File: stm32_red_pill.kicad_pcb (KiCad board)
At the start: 2 copper layers, 59 x 31 mm, 29 parts, among them J1 USB_B_Micro, J2 Conn_01x18, J3 Conn_01x18, SW1 SW_SPDT, U1 STM32F103C8T6, U2 AMS1117-3.3, Y1 16MHZ

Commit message: update
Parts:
- removed SW1: SW_SPDT, Button_Switch_SMD:SW_SPDT_PCM12
- added G***: LOGO, LOGO, F.Cu at (89.0, 101.7)
- added J4: Conn_02x02_Top_Bottom, Connector_PinHeader_2.54mm:PinHeader_2x02_P2.54mm_Vertical, F.Cu at (135.9, 96.8)
- moved R1 17.6 mm to (116.0, 100.5), turned to -135 degrees
- moved C7 2.05 mm to (98.3, 103.9), turned to -45 degrees
- moved C11 1.85 mm to (100.8, 96.1)
- moved C10 1.85 mm to (100.8, 94.1)
- moved Y1 1.85 mm to (98.3, 94.9)
- moved R3 1.31 mm to (118.9, 102.5), turned to 135 degrees
- moved FB1 0.90 mm to (97.8, 105.2), turned to -45 degrees
- moved D1 0.68 mm to (119.5, 101.2)
- moved C8 0.21 mm to (97.4, 106.5), turned to 135 degrees
- moved C2 0.06 mm to (111.5, 96.0)
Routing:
- net /SW_BOOT0: track 1.56 -> 21.3 mm, vias 0 -> 2
- net /BOOT0: track 25.6 -> 7.74 mm, vias 2 -> 0
- net +3.3V: track 85.7 -> 93.3 mm
- net /PA2: track 24.1 -> 22.0 mm
- net /HSE_OUT: track 10.1 -> 8.29 mm
- net /HSE_IN: track 13.4 -> 11.5 mm
- net /PA1: track 22.4 -> 20.7 mm
- net GND: track 30.9 -> 29.5 mm, vias 20 -> 24
- net /PA0: track 21.5 -> 20.2 mm
- net +3.3VA: track 12.4 -> 11.4 mm
- net /PB9: track 13.7 -> 14.4 mm, vias 2 -> 0
- net /PA13: track 22.2 -> 22.6 mm, vias 2 -> 1
- net VBUS: track 11.2 -> 11.1 mm, vias 7 -> 6
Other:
- board text added: "Designed by Philip V1.0"

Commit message: update
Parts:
- moved C8 1.68 mm to (98.8, 105.5)
- moved FB1 1.68 mm to (99.2, 104.2)
- moved C7 1.68 mm to (99.7, 102.9)
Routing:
- net +3.3VA: track 11.4 -> 9.66 mm
- net +3.3V: track 93.3 -> 92.3 mm
- net /SW_BOOT0: track 21.3 -> 21.9 mm

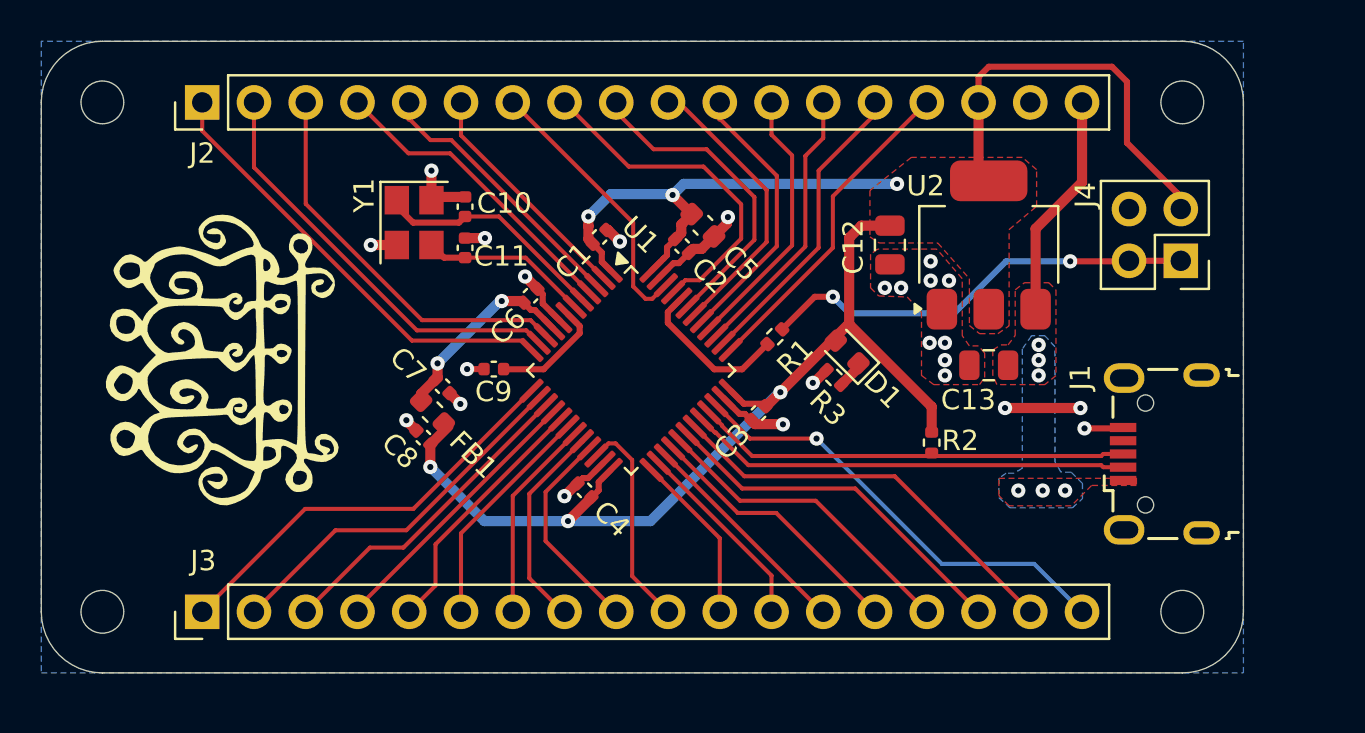
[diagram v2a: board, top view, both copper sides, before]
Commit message: 4 layer design
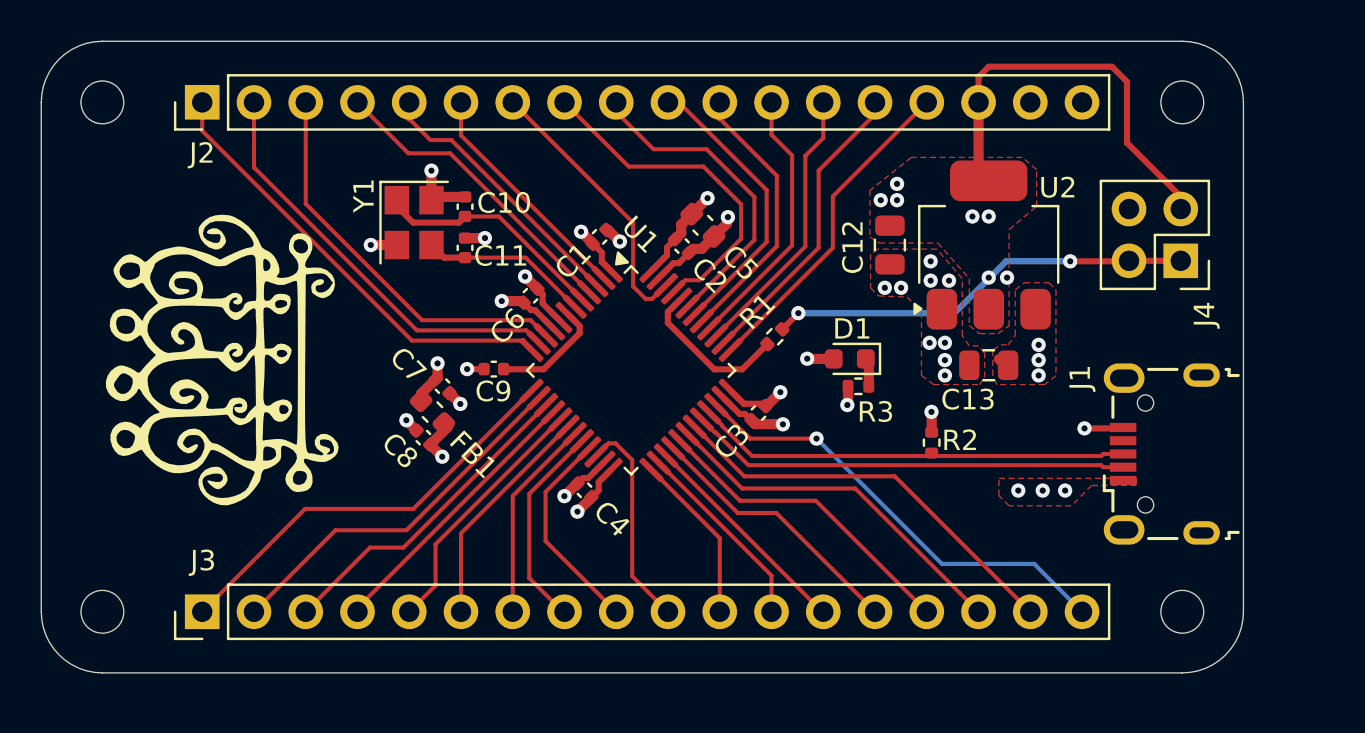
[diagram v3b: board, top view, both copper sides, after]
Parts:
- moved R3 1.28 mm to (120.1, 102.9), turned to 180 degrees
- moved D1 0.36 mm to (119.7, 101.6), turned to 180 degrees
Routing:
- net +3.3V: track 92.3 -> 38.0 mm, vias 6 -> 14
- net GND: track 29.1 -> 25.4 mm, vias 24 -> 22
- net VBUS: track 11.1 -> 13.4 mm
- net /SW_BOOT0: track 21.9 -> 21.3 mm
- added copper zone on In2.Cu, net +3.3V
- added copper zone on In1.Cu, net GND
- added copper zone on In2.Cu, net VBUS
- removed copper zone on B.Cu, net GND
- removed copper zone on B.Cu, net VBUS
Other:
- copper layers 2 -> 4

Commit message: lol
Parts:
- removed the G*** at (89.0, 101.7)
- added G*** (x2): LOGO, LOGO, F.Cu at (92.9, 103.2)
- D1: value BLUE -> RED
- moved R1 4.68 mm to (119.8, 103.3)
- moved D1 4.64 mm to (124.0, 103.2)
- moved R3 4.64 mm to (124.5, 104.5)
- moved H1 4.57 mm to (87.0, 91.3)
- moved H2 4.57 mm to (139.9, 91.3)
- moved C2 4.26 mm to (115.4, 97.7)
- moved C9 4.26 mm to (106.2, 103.7)
- moved C3 4.26 mm to (119.2, 105.8)
- moved C4 4.26 mm to (110.6, 109.6)
- moved C5 4.26 mm to (116.4, 96.6)
- moved C6 4.26 mm to (108.0, 100.1)
- moved U1 4.26 mm to (112.9, 103.8)
- moved C1 4.26 mm to (111.3, 97.2)
- moved C12 4.26 mm to (125.6, 97.6)
- moved C13 4.26 mm to (130.4, 103.5)
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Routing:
- net +3.3V: track 38.0 -> 18.4 mm
- net /PA13: track 22.6 -> 26.6 mm
- net VBUS: track 13.4 -> 17.0 mm
- net /PA2: track 22.0 -> 24.7 mm
- net /PA1: track 20.7 -> 22.7 mm
- net +3.3VA: track 9.66 -> 11.0 mm
- net /PA0: track 20.2 -> 21.3 mm
- net /SW_BOOT0: track 21.3 -> 22.2 mm, vias 2 -> 1
- net /BOOT0: track 7.74 -> 7.08 mm
- net /HSE_OUT: track 8.29 -> 8.90 mm
- net /HSE_IN: track 11.5 -> 12.1 mm
- net GND: track 25.4 -> 24.8 mm
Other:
- board size 59 x 31 mm -> 59 x 29.6 mm
- board text added: "+3.3V"
- board text added: "BOOT0"
- board text added: "GND"
- board text added: "STM32 Chaos Pill V1.0 Designed by Philip Perpetual Chaos"
- board text added: "VBUS"
- board text removed: "Designed by Philip V1.0"
